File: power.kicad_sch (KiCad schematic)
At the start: 18 parts, among them J2 USB_C_Receptacle_USB2.0_16P, J3 Conn_01x02_Pin, U4 USBLC6-2SC6, U5 BQ24090DGQ, U6 MAX17048G, U7 TPS7A0508PDBZ

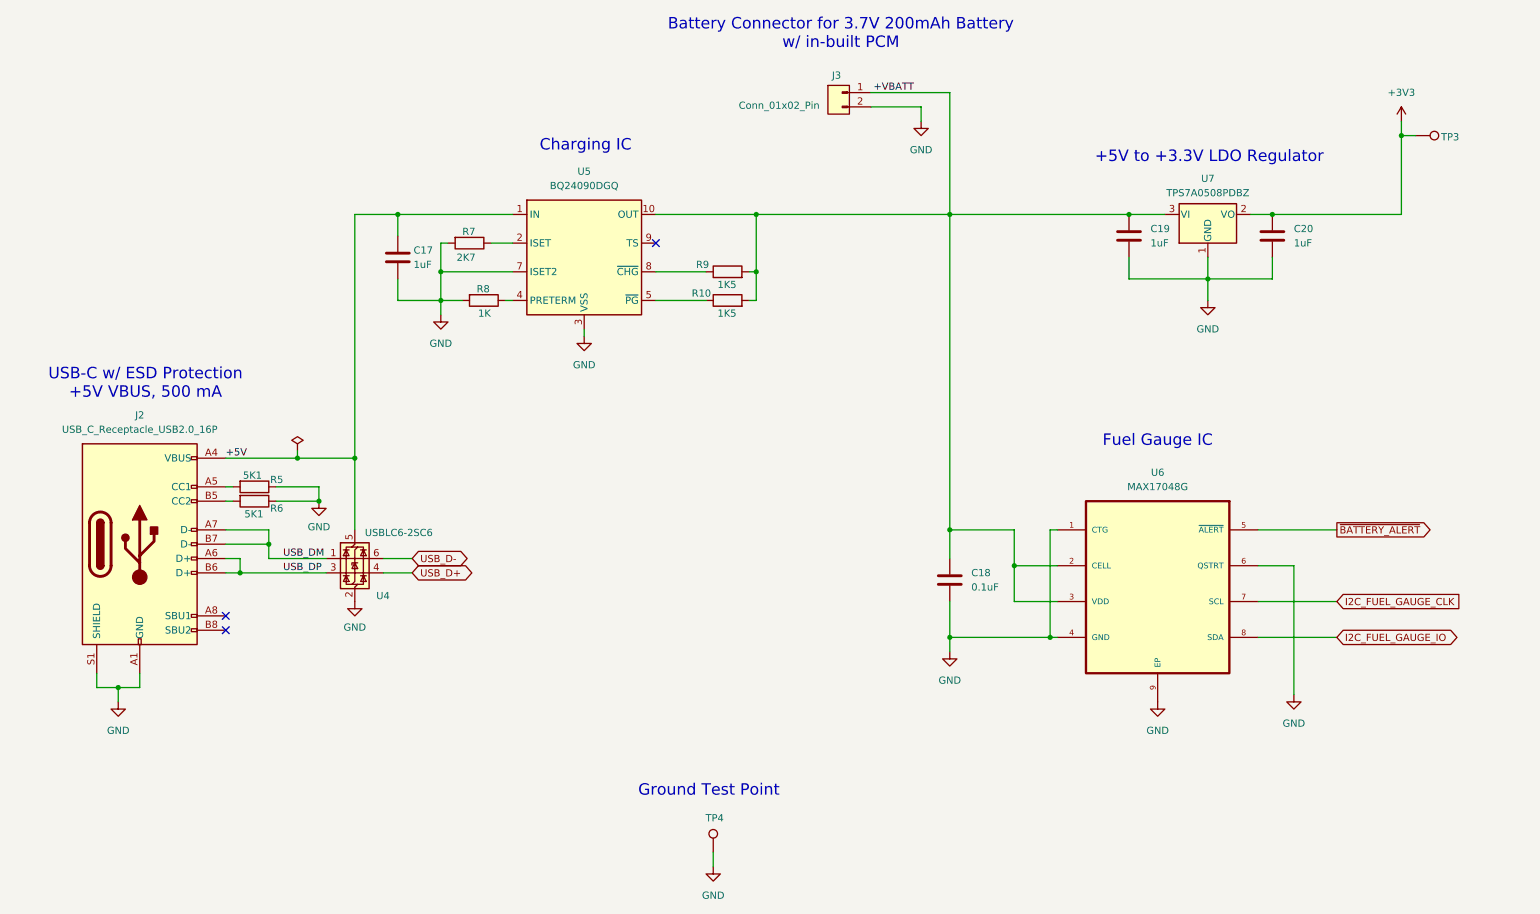
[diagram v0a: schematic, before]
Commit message: changed fram for ic flash memory
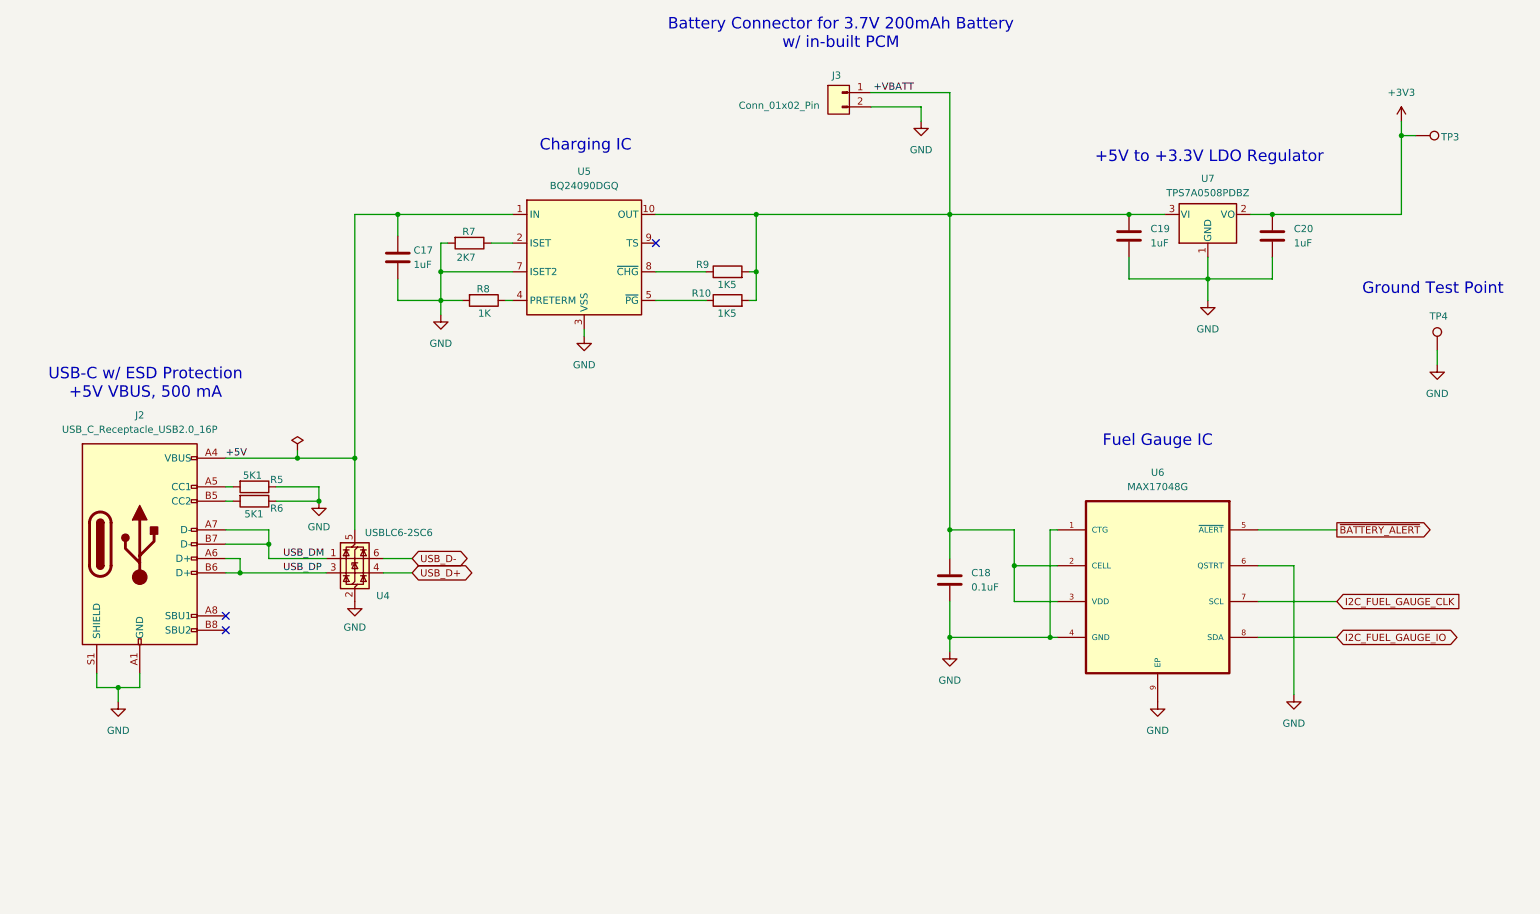
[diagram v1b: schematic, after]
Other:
- moved on the sheet: TP4
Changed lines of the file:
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@@
 	(text "Ground Test Point"
 		(exclude_from_sim no)
-		(at 136.398 157.988 0)
+		(at 264.668 69.088 0)
 		(effects
 			(font
@@
 	(wire
 		(pts
-			(xy 137.16 168.91) (xy 137.16 171.45)
+			(xy 265.43 80.01) (xy 265.43 82.55)
 		)
 		(stroke
@@
 	(symbol
 		(lib_id "Connector:TestPoint")
-		(at 137.16 168.91 0)
+		(at 265.43 80.01 0)
 		(unit 1)
 		(exclude_from_sim no)
@@
 		(dnp no)
 		(property "Reference" "TP4"
-			(at 137.414 162.814 0)
+			(at 265.684 73.914 0)
 			(effects
 				(font
@@
 		)
 		(property "Value" "~"
-			(at 136.652 166.878 90)
+			(at 264.922 77.978 90)
 			(effects
 				(font
@@
 		)
 		(property "Footprint" "TestPoint:TestPoint_Pad_D1.0mm"
-			(at 142.24 168.91 0)
+			(at 270.51 80.01 0)
 			(effects
 				(font
@@
 		)
 		(property "Datasheet" "~"
-			(at 142.24 168.91 0)
+			(at 270.51 80.01 0)
 			(effects
 				(font
@@
 		)
 		(property "Description" "test point"
-			(at 137.16 168.91 0)
+			(at 265.43 80.01 0)
 			(effects
 				(font
@@
 	(symbol
 		(lib_id "power:GND")
-		(at 137.16 171.45 0)
+		(at 265.43 82.55 0)
 		(unit 1)
 		(exclude_from_sim no)
@@
 		(fields_autoplaced yes)
 		(property "Reference" "#PWR08"
-			(at 137.16 177.8 0)
+			(at 265.43 88.9 0)
 			(effects
 				(font
@@
 		)
 		(property "Value" "GND"
-			(at 137.16 176.53 0)
+			(at 265.43 87.63 0)
 			(effects
 				(font
@@
 		)
 		(property "Footprint" ""
-			(at 137.16 171.45 0)
+			(at 265.43 82.55 0)
 			(effects
 				(font
@@
 		)
 		(property "Datasheet" ""
-			(at 137.16 171.45 0)
+			(at 265.43 82.55 0)
 			(effects
 				(font
@@
 		)
 		(property "Description" "Power symbol creates a global label with name \"GND\" , ground"
-			(at 137.16 171.45 0)
+			(at 265.43 82.55 0)
 			(effects
 				(font

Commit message: Choose footprints for all parts
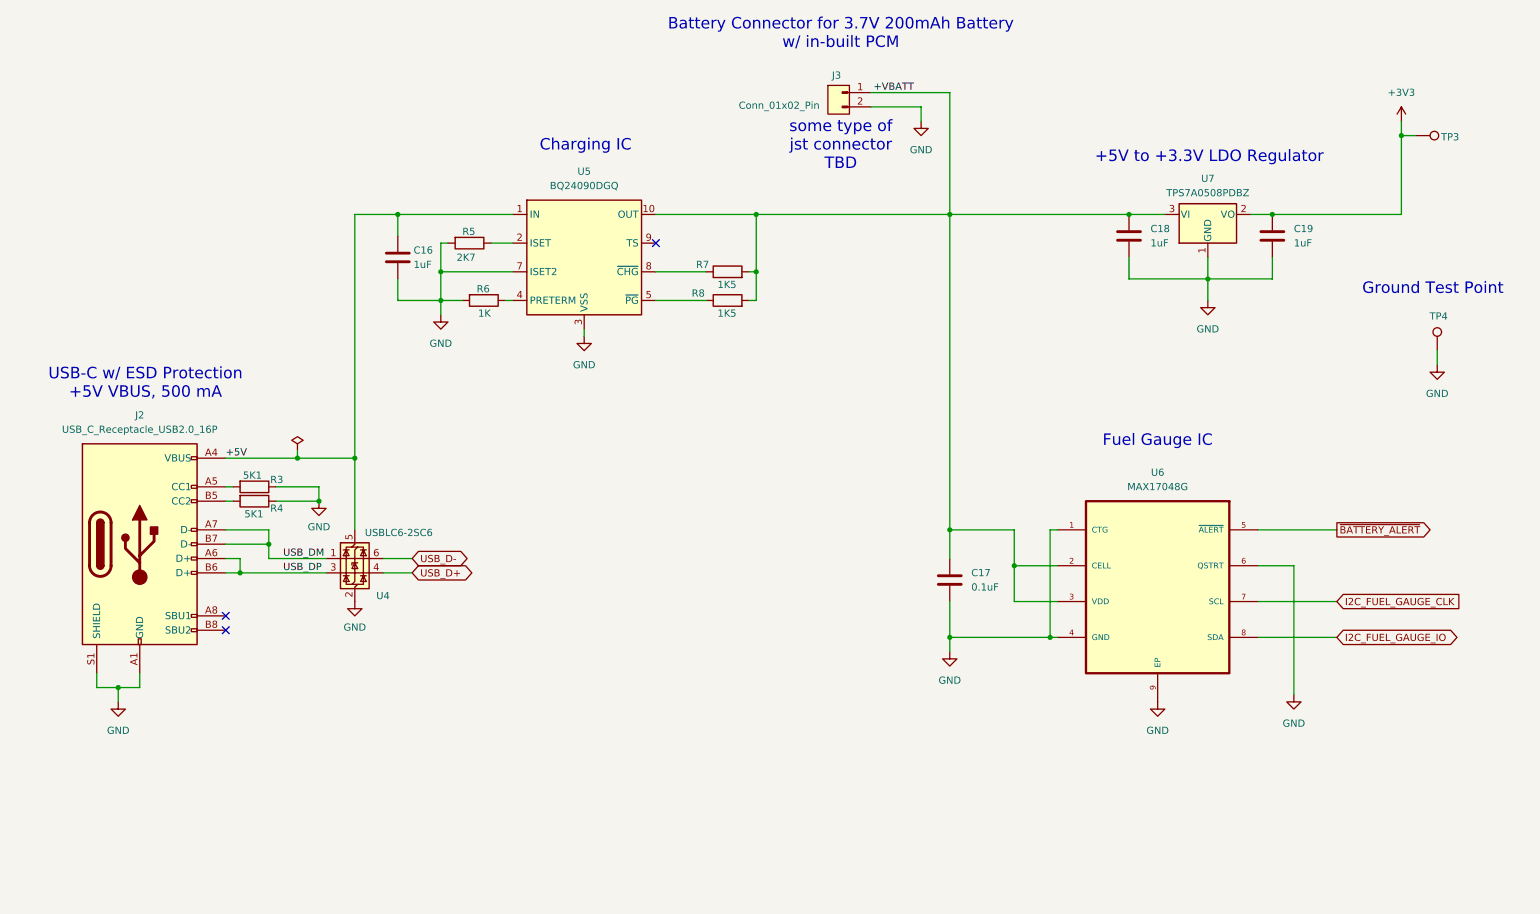
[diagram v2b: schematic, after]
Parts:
- C16: renamed from C17; footprint (none) -> Capacitor_SMD:C_0402_1005Metric
- C17: renamed from C18; footprint (none) -> Capacitor_SMD:C_0402_1005Metric
- C18: renamed from C19; footprint (none) -> Capacitor_SMD:C_0402_1005Metric
- C19: renamed from C20; footprint (none) -> Capacitor_SMD:C_0402_1005Metric
- J3: footprint (none) -> Connector_JST:JST_PH_B2B-PH-K_1x02_P2.00mm_Vertical
- R3: renamed from R5; footprint (none) -> Resistor_SMD:R_0402_1005Metric
- R4: renamed from R6; footprint (none) -> Resistor_SMD:R_0402_1005Metric
- R5: renamed from R7; footprint (none) -> Resistor_SMD:R_0402_1005Metric
- R6: renamed from R8; footprint (none) -> Resistor_SMD:R_0402_1005Metric
- R7: renamed from R9; footprint (none) -> Resistor_SMD:R_0402_1005Metric
- R8: renamed from R10; footprint (none) -> Resistor_SMD:R_0402_1005Metric
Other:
- note added: "some type of jst connector TBD"

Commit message: Changed from stm32wb -> nRF52 module
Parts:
- U5: footprint LibraryFootprints:MLPF-WB55-01E3 -> Package_SO:HVSSOP-10-1EP_3x3mm_P0.5mm_EP1.83x1.89mm
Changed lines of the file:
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@@
 			)
 		)
-		(property "Footprint" "LibraryFootprints:MLPF-WB55-01E3"
+		(property "Footprint" "Package_SO:HVSSOP-10-1EP_3x3mm_P0.5mm_EP1.83x1.89mm"
 			(at 114.3 63.5 0)
 			(effects

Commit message: Layout progress
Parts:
- removed C16: 1uF, Capacitor_SMD:C_0402_1005Metric, symbol Device:C
- removed J2: USB_C_Receptacle_USB2.0_16P, Connector_USB:USB_C_Receptacle_Molex_105450-0101, symbol Connector:USB_C_Receptacle_USB2.0_16P
- removed R3, R4: 5K1, Resistor_SMD:R_0402_1005Metric, symbol Device:R
- removed R5: 2K7, Resistor_SMD:R_0402_1005Metric, symbol Device:R
- removed R6: 1K, Resistor_SMD:R_0402_1005Metric, symbol Device:R
- removed R7, R8: 1K5, Resistor_SMD:R_0402_1005Metric, symbol Device:R
- removed U4: USBLC6-2SC6, Package_TO_SOT_SMD:SOT-23-6, symbol Power_Protection:USBLC6-2SC6
- removed U5: BQ24090DGQ, Package_SO:HVSSOP-10-1EP_3x3mm_P0.5mm_EP1.83x1.89mm, symbol Battery_Management:BQ24090DGQ
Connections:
- no-connect marks 3 -> 0
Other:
- note removed: "Charging IC"
- note removed: "USB-C w/ ESD Protection +5V VBUS, 500 mA"
